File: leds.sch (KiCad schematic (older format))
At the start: 66 parts

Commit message: Remap project symbols
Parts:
- DB02, DB04, DB041, DB05, DB051, DB06, DB07, DB09, DB10, DB101, DB102, DB11, DB14, DB15, DB151, DB16, DB17, DB19, DB21, DB22, DB23, DB24, DB26, DB27, DB28, DB29, DB30, DB301, DB302, DB31, DB32, DB33, DB34, DB36, DB37, DB38, DB39, DB41, DB42, DB43, DB44, DB46, DB47, DB48, DB49, DB50, DB51, DB52, DB53, DB54, DB55, DB551, DB56, DB57, DB58, DB59, DB61, DB62, DB63, DB66, DB661, DB67, DB68, DB681, DB682, DB69: symbol LED -> device:LED
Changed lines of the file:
@@
-EESchema Schematic File Version 2
-LIBS:power
-LIBS:mx1a-simple
-LIBS:aker
-LIBS:atmega32u4
-LIBS:dtsjw
-LIBS:oupiin_usb
-LIBS:device
-LIBS:conn
-LIBS:keyboard-cache
-EELAYER 25 0
+EESchema Schematic File Version 4
+EELAYER 30 0
 EELAYER END
 $Descr A4 11693 8268
@@
 $EndDescr
 $Comp
-L LED DB21
+L device:LED DB21
 U 1 1 51900721
 P 4450 1950
@@
 $EndComp
 $Comp
-L LED DB26
+L device:LED DB26
 U 1 1 51900730
 P 5000 1950
@@
 $EndComp
 $Comp
-L LED DB31
+L device:LED DB31
 U 1 1 51900737
 P 5550 1950
@@
 $EndComp
 $Comp
-L LED DB36
+L device:LED DB36
 U 1 1 5190073E
 P 6100 1950
@@
 $EndComp
 $Comp
-L LED DB06
+L device:LED DB06
 U 1 1 5190074C
 P 2800 1950
@@
 $EndComp
 $Comp
-L LED DB11
+L device:LED DB11
 U 1 1 51900753
 P 3350 1950
@@
 $EndComp
 $Comp
-L LED DB16
+L device:LED DB16
 U 1 1 5190075A
 P 3900 1950
@@
 $EndComp
 $Comp
-L LED DB61
+L device:LED DB61
 U 1 1 51900761
 P 8850 1950
@@
 $EndComp
 $Comp
-L LED DB66
+L device:LED DB66
 U 1 1 51900768
 P 9400 1950
@@
 $EndComp
 $Comp
-L LED DB41
+L device:LED DB41
 U 1 1 5190077D
 P 6650 1950
@@
 $EndComp
 $Comp
-L LED DB46
+L device:LED DB46
 U 1 1 51900784
 P 7200 1950
@@
 $EndComp
 $Comp
-L LED DB51
+L device:LED DB51
 U 1 1 5190078B
 P 7750 1950
@@
 $EndComp
 $Comp
-L LED DB56
+L device:LED DB56
 U 1 1 51900792
 P 8300 1950
@@
 $EndComp
 $Comp
-L LED DB22
+L device:LED DB22
 U 1 1 51900799
 P 4450 2850
@@
 $EndComp
 $Comp
-L LED DB27
+L device:LED DB27
 U 1 1 519007A0
 P 5000 2850
@@
 $EndComp
 $Comp
-L LED DB32
+L device:LED DB32
 U 1 1 519007A7
 P 5550 2850
@@
 $EndComp
 $Comp
-L LED DB37
+L device:LED DB37
 U 1 1 519007AE
 P 6100 2850
@@
 $EndComp
 $Comp
-L LED DB02
+L device:LED DB02
 U 1 1 519007B5
 P 2250 2850
@@
 $EndComp
 $Comp
-L LED DB07
+L device:LED DB07
 U 1 1 519007BC
 P 2800 2850
@@
 $EndComp
 $Comp
-L LED DB17
+L device:LED DB17
 U 1 1 519007CA
 P 3900 2850
@@
 $EndComp
 $Comp
-L LED DB62
+L device:LED DB62
 U 1 1 519007D1
 P 8850 2850
@@
 $EndComp
 $Comp
-L LED DB67
+L device:LED DB67
 U 1 1 519007D8
 P 9400 2850
@@
 $EndComp
 $Comp
-L LED DB42
+L device:LED DB42
 U 1 1 519007E6
 P 6650 2850
@@
 $EndComp
 $Comp
-L LED DB47
+L device:LED DB47
 U 1 1 519007ED
 P 7200 2850
@@
 $EndComp
 $Comp
-L LED DB52
+L device:LED DB52
 U 1 1 519007F4
 P 7750 2850
@@
 $EndComp
 $Comp
-L LED DB57
+L device:LED DB57
 U 1 1 519007FB
 P 8300 2850
@@
 $EndComp
 $Comp
-L LED DB23
+L device:LED DB23
 U 1 1 51900802
 P 4450 3500
@@
 $EndComp
 $Comp
-L LED DB28
+L device:LED DB28
 U 1 1 51900809
 P 5000 3500
@@
 $EndComp
 $Comp
-L LED DB33
+L device:LED DB33
 U 1 1 51900810
 P 5550 3500
@@
 $EndComp
 $Comp
-L LED DB38
+L device:LED DB38
 U 1 1 51900817
 P 6100 3500
@@
 $EndComp
 $Comp
-L LED DB63
+L device:LED DB63
 U 1 1 5190083A
 P 8850 3500
@@
 $EndComp
 $Comp
-L LED DB68
+L device:LED DB68
 U 1 1 51900841
 P 9400 3500
@@
 $EndComp
 $Comp
-L LED DB43
+L device:LED DB43
 U 1 1 5190084F
 P 6650 3500
@@
 $EndComp
 $Comp
-L LED DB48
+L device:LED DB48
 U 1 1 51900856
 P 7200 3500
@@
 $EndComp
 $Comp
-L LED DB53
+L device:LED DB53
 U 1 1 5190085D
 P 7750 3500
@@
 $EndComp
 $Comp
-L LED DB58
+L device:LED DB58
 U 1 1 51900864
 P 8300 3500
@@
 $EndComp
 $Comp
-L LED DB24
+L device:LED DB24
 U 1 1 5190086B
 P 4450 4650
@@
 $EndComp
 $Comp
-L LED DB29
+L device:LED DB29
 U 1 1 51900872
 P 5000 4650
@@
 $EndComp
 $Comp
-L LED DB34
+L device:LED DB34
 U 1 1 51900879
 P 5550 4650
@@
 $EndComp
 $Comp
-L LED DB39
+L device:LED DB39
 U 1 1 51900880
 P 6100 4650
@@
 $EndComp
 $Comp
-L LED DB04
+L device:LED DB04
 U 1 1 51900887
 P 2250 4650
@@
 $EndComp
 $Comp
-L LED DB09
+L device:LED DB09
 U 1 1 5190088E
 P 2800 4650
@@
 $EndComp
 $Comp
-L LED DB14
+L device:LED DB14
 U 1 1 51900895
 P 3350 4650
@@
 $EndComp
 $Comp
-L LED DB19
+L device:LED DB19
 U 1 1 5190089C
 P 3900 4650
@@
 $EndComp
 $Comp
-L LED DB44
+L device:LED DB44
 U 1 1 519008B8
 P 6650 4650
@@
 $EndComp
 $Comp
-L LED DB49
+L device:LED DB49
 U 1 1 519008BF
 P 7200 4650
@@
 $EndComp
 $Comp
-L LED DB54
+L device:LED DB54
 U 1 1 519008C6
 P 7750 4650
@@
 $EndComp
 $Comp
-L LED DB59
+L device:LED DB59
 U 1 1 519008CD
 P 8300 4650
@@
 $EndComp
 $Comp
-L LED DB05
+L device:LED DB05
 U 1 1 519008F0
 P 2250 5550
@@
 $EndComp
 $Comp
-L LED DB10
+L device:LED DB10
 U 1 1 519008F7
 P 2800 5550
@@
 $EndComp
 $Comp
-L LED DB15
+L device:LED DB15
 U 1 1 519008FE
 P 3350 5550
@@
 $EndComp
 $Comp
-L LED DB50
+L device:LED DB50
 U 1 1 51900928
 P 7200 5550
@@
 $EndComp
 $Comp
-L LED DB55
+L device:LED DB55
 U 1 1 5190092F
 P 7750 5550
@@
 $EndComp
 $Comp
-L LED DB30
+L device:LED DB30
 U 1 1 519008DB
 P 5000 5550
@@
 $EndComp
 $Comp
-L LED DB551
+L device:LED DB551
 U 1 1 51C02CCF
 P 7750 5800
@@
 $EndComp
 $Comp
-L LED DB301
+L device:LED DB301
 U 1 1 51C0300D
 P 5000 5800
@@
 $EndComp
 $Comp
-L LED DB302
+L device:LED DB302
 U 1 1 51C03013
 P 5000 6050
@@
 $EndComp
 $Comp
-L LED DB051
+L device:LED DB051
 U 1 1 51C0378E
 P 2250 5800
@@
 $EndComp
 $Comp
-L LED DB101
+L device:LED DB101
 U 1 1 51C065B4
 P 2800 5800
@@
 $EndComp
 $Comp
-L LED DB102
+L device:LED DB102
 U 1 1 51C065BA
 P 2800 6050
@@
 $EndComp
 $Comp
-L LED DB151
+L device:LED DB151
 U 1 1 51C06955
 P 3350 5800
@@
 esc
 $Comp
-L LED DB69
+L device:LED DB69
 U 1 1 51C41A1A
 P 9400 4650
@@
 Fn
 $Comp
-L LED DB041
+L device:LED DB041
 U 1 1 51D98243
 P 2250 4900
@@
 Connection ~ 2050 4900
 $Comp
-L LED DB661
+L device:LED DB661
 U 1 1 51D9840C
 P 9400 2200
@@
 Connection ~ 9200 2200
 $Comp
-L LED DB681
+L device:LED DB681
 U 1 1 51D988E8
 P 9400 3750
@@
 $EndComp
 $Comp
-L LED DB682
+L device:LED DB682
 U 1 1 51D988EE
 P 9400 4000

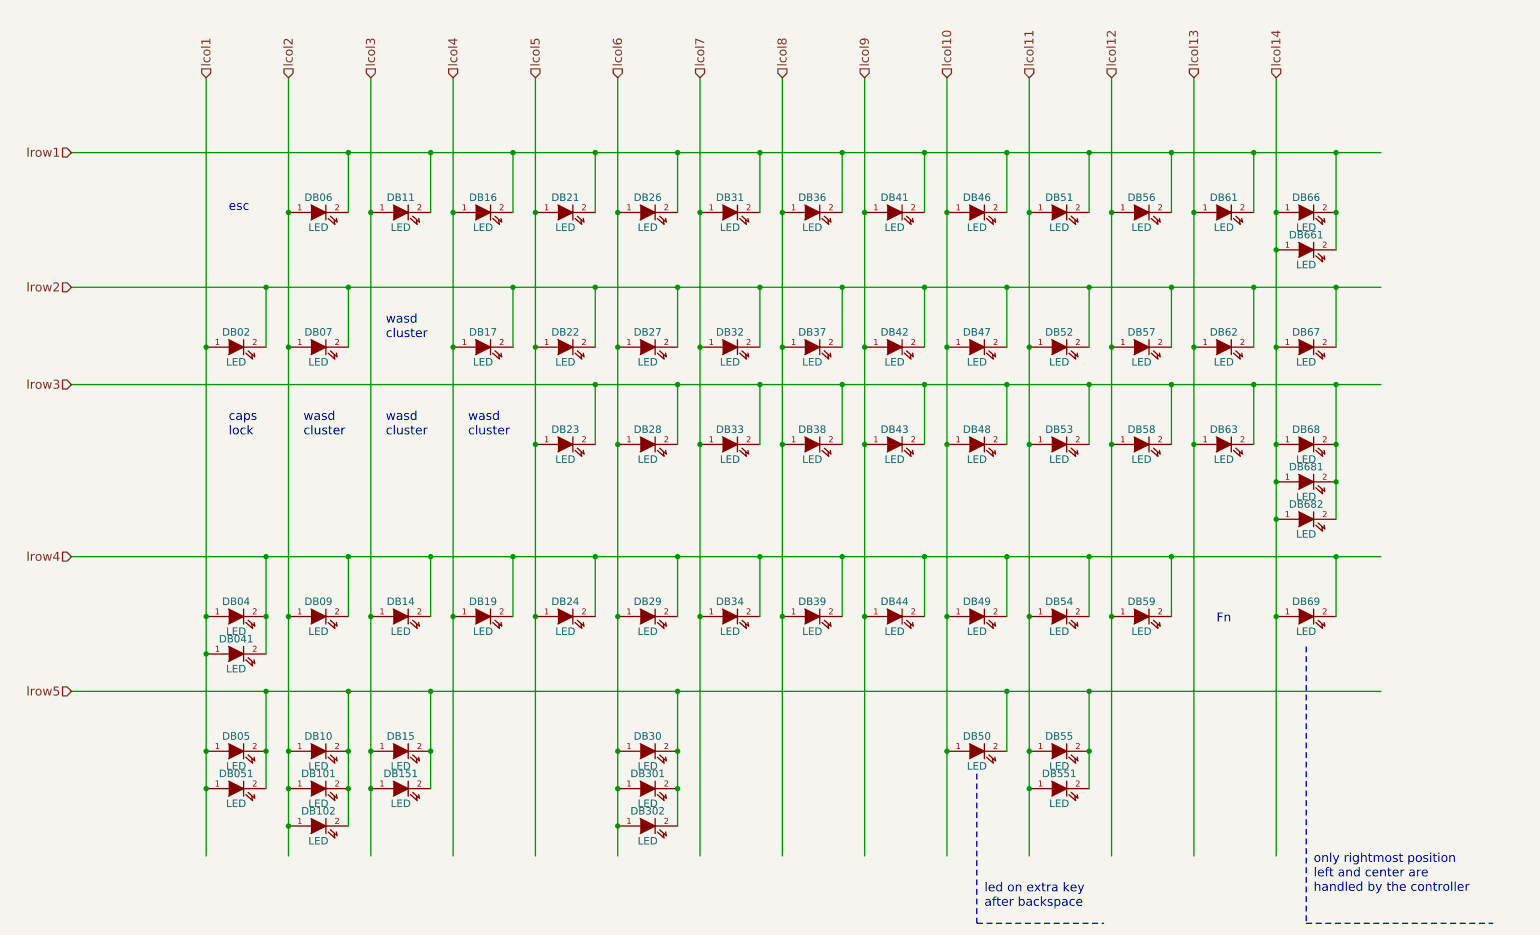
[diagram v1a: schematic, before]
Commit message: Remove SW50 from matrix and leds
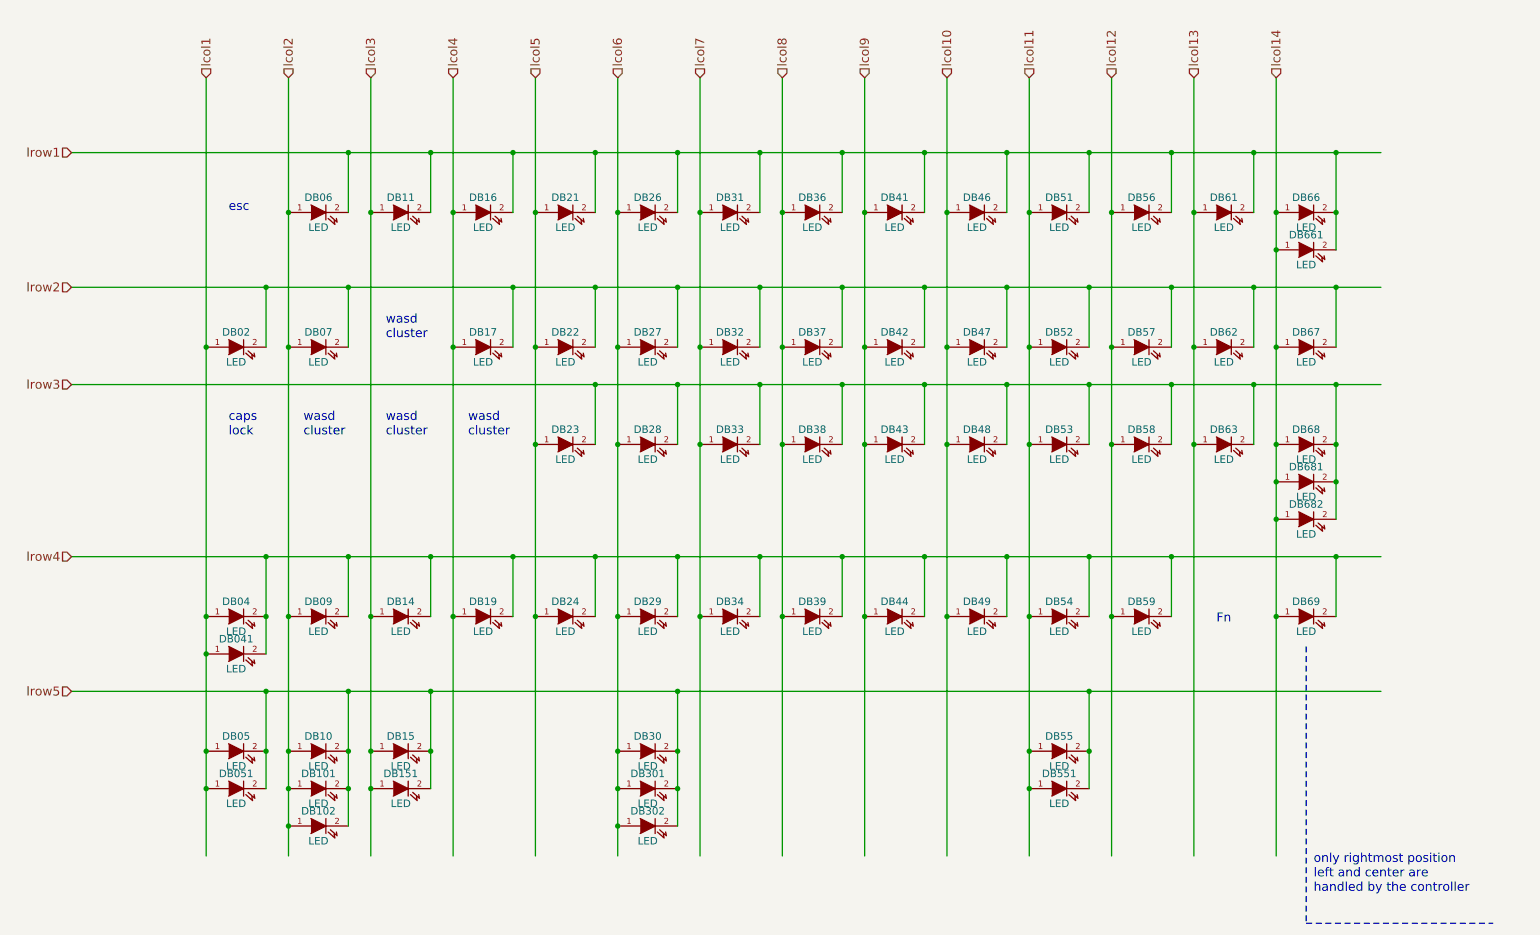
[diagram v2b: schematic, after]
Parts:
- removed DB50: LED, mx1a:MX1A-led_no3d, symbol device:LED
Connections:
- wire segments 74 -> 203
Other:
- note removed: "led on extra key\nafter backspace"

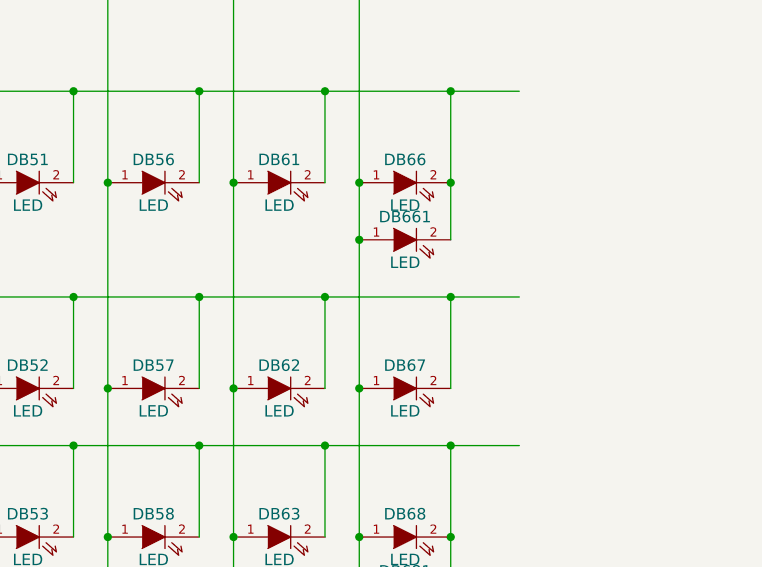
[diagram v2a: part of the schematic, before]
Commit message: Remove SW661
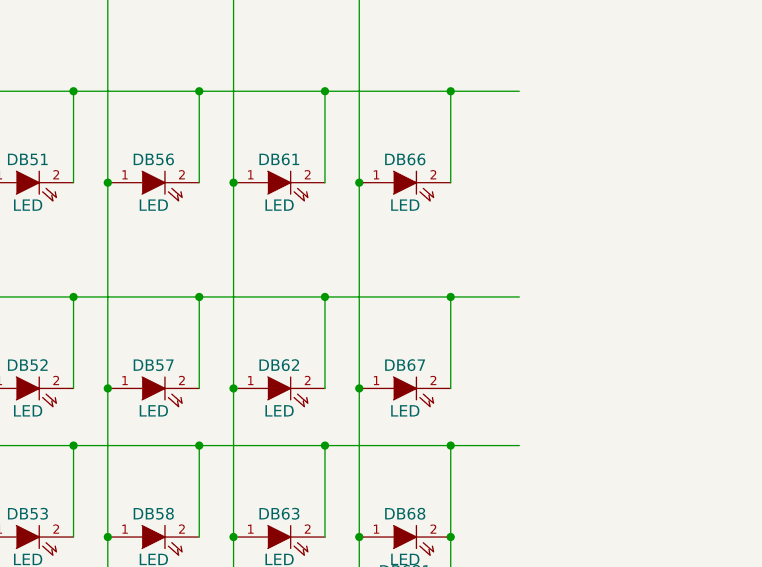
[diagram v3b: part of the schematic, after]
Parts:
- removed DB661: LED, mx1a:MX1A-led_no3d, symbol device:LED
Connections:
- wire segments 203 -> 201
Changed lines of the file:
@@
 Connection ~ 2050 4900
-$Comp
-L device:LED DB661
-U 1 1 51D9840C
-P 9400 2200
-F 0 "DB661" H 9400 2300 50  0000 C CNN
-F 1 "LED" H 9400 2100 50  0000 C CNN
-F 2 "mx1a:MX1A-led_no3d" H 9400 2200 60  0001 C CNN
-F 3 "" H 9400 2200 60  0001 C CNN
-	1    9400 2200
-	1    0    0    -1
-$EndComp
-Connection ~ 9600 1950
-Connection ~ 9200 2200
 $Comp
 L device:LED DB681
@@
 	9050 1550 9600 1550
 Wire Wire Line
-	9200 1950 9200 2200
-Wire Wire Line
 	9600 1550 9900 1550
 Wire Wire Line
@@
 	2050 4900 2050 5550
 Wire Wire Line
-	9600 1950 9600 2200
-Wire Wire Line
-	9200 2200 9200 2850
-Wire Wire Line
 	9600 3500 9600 3750
 Wire Wire Line
@@
 Wire Wire Line
 	5200 5150 7950 5150
+Wire Wire Line
+	9200 1950 9200 2850
 $EndSCHEMATC

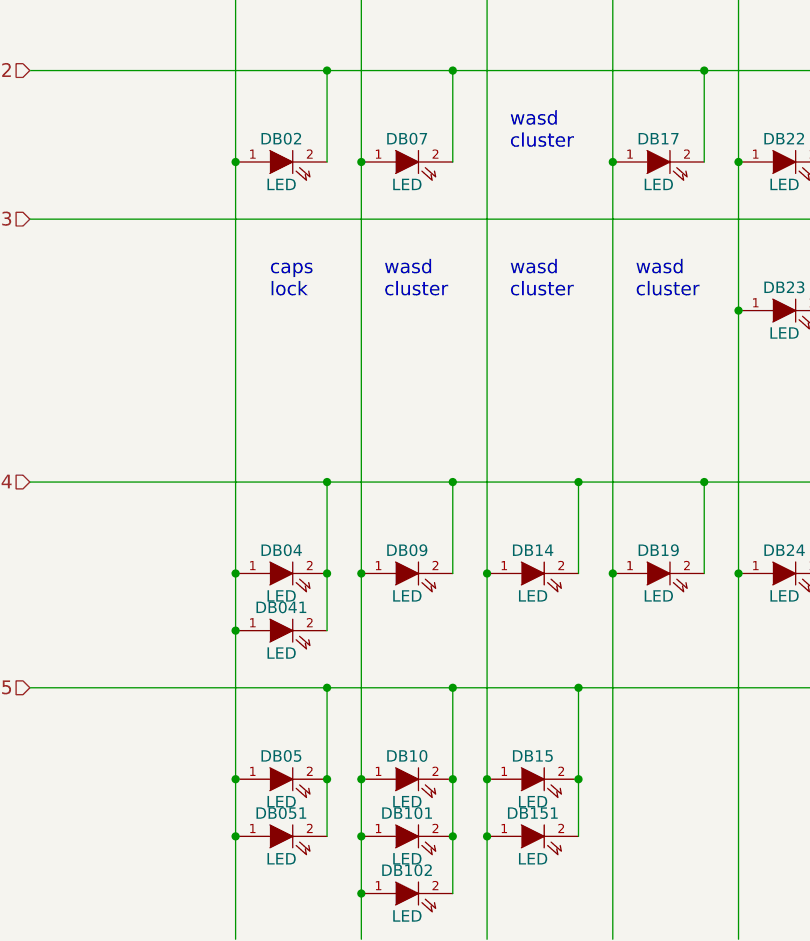
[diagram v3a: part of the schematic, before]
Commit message: Remove SW09 and SW041
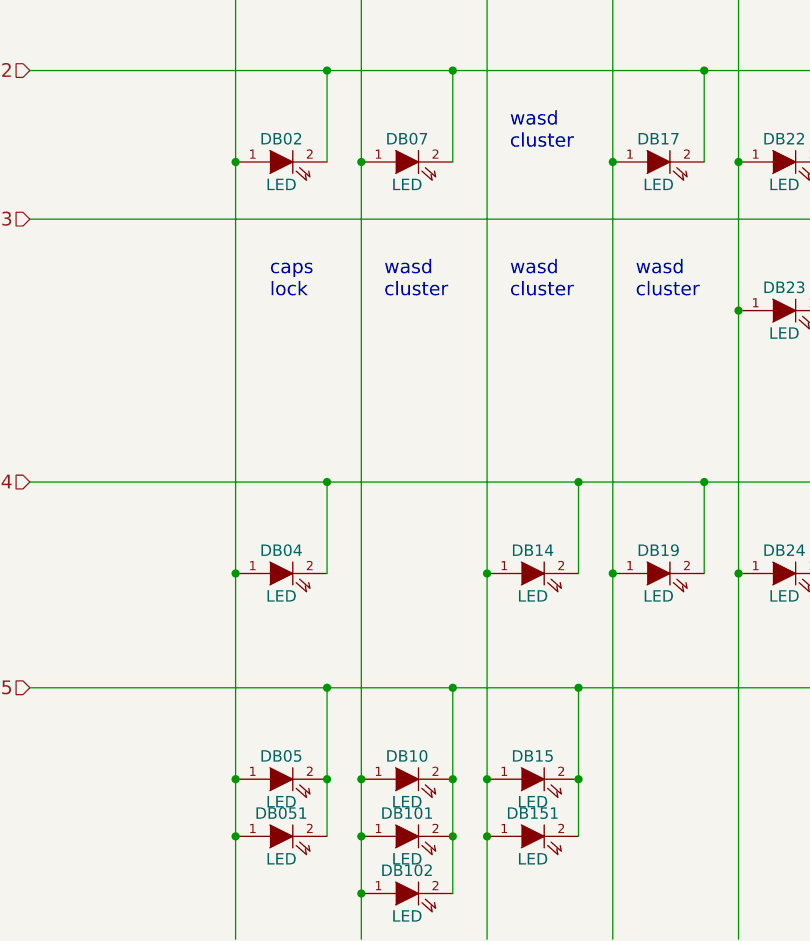
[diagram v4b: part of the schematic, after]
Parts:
- removed DB041, DB09: LED, mx1a:MX1A-led_no3d, symbol device:LED
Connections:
- wire segments 201 -> 196
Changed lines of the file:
@@
-$EndComp
-$Comp
-L device:LED DB09
-U 1 1 5190088E
-P 2800 4650
-F 0 "DB09" H 2800 4750 50  0000 C CNN
-F 1 "LED" H 2800 4550 50  0000 C CNN
-F 2 "mx1a:MX1A-led_no3d" H 2800 4650 60  0001 C CNN
-F 3 "" H 2800 4650 60  0001 C CNN
-	1    2800 4650
-	1    0    0    -1
 $EndComp
 $Comp
@@
 Wire Wire Line
 	2450 4250 2450 4650
-Wire Wire Line
-	3000 4250 3000 4650
 Wire Wire Line
 	3550 4250 3550 4650
@@
 Connection ~ 2050 4650
 Connection ~ 2450 4250
-Connection ~ 2600 4650
-Connection ~ 3000 4250
 Connection ~ 3150 4650
 Connection ~ 3550 4250
@@
 Fn
 $Comp
-L device:LED DB041
-U 1 1 51D98243
-P 2250 4900
-F 0 "DB041" H 2250 5000 50  0000 C CNN
-F 1 "LED" H 2250 4800 50  0000 C CNN
-F 2 "mx1a:MX1A-led_no3d" H 2250 4900 60  0001 C CNN
-F 3 "" H 2250 4900 60  0001 C CNN
-	1    2250 4900
-	1    0    0    -1
-$EndComp
-Connection ~ 2450 4650
-Connection ~ 2050 4900
-$Comp
 L device:LED DB681
 U 1 1 51D988E8
@@
 	2450 2450 3000 2450
 Wire Wire Line
-	2600 2850 2600 4650
-Wire Wire Line
 	3000 2450 4100 2450
 Wire Wire Line
@@
 	9600 2450 9900 2450
 Wire Wire Line
-	2050 4650 2050 4900
-Wire Wire Line
-	2450 4250 3000 4250
-Wire Wire Line
-	2600 4650 2600 5550
-Wire Wire Line
-	3000 4250 3550 4250
-Wire Wire Line
 	3150 4650 3150 5550
 Wire Wire Line
@@
 	9600 4250 9900 4250
 Wire Wire Line
-	2450 4650 2450 4900
-Wire Wire Line
-	2050 4900 2050 5550
-Wire Wire Line
 	9600 3500 9600 3750
 Wire Wire Line
@@
 Wire Wire Line
 	9200 1950 9200 2850
+Wire Wire Line
+	2600 2850 2600 5550
+Wire Wire Line
+	2450 4250 3550 4250
+Wire Wire Line
+	2050 4650 2050 5550
 $EndSCHEMATC

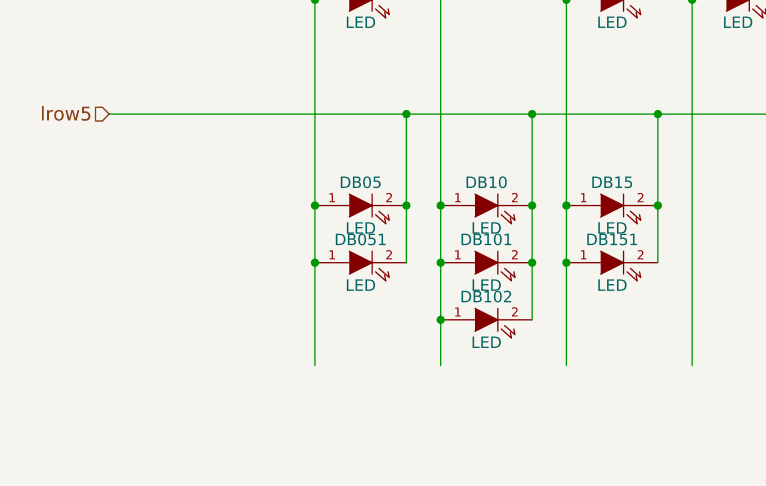
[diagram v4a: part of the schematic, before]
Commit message: Remove SW0512
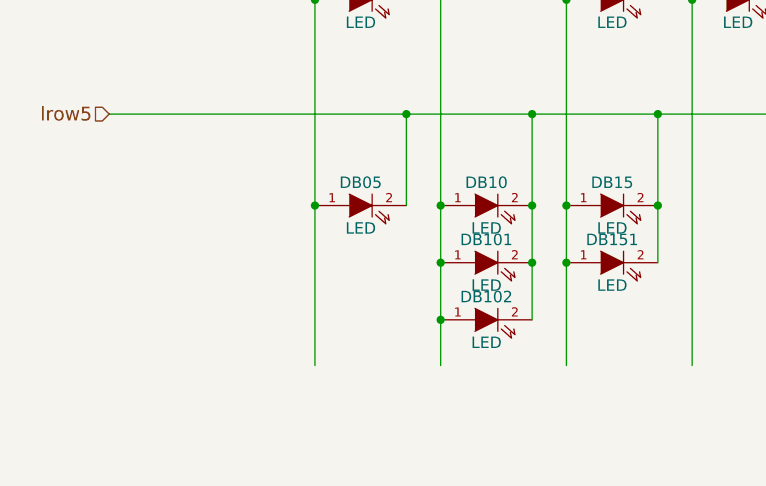
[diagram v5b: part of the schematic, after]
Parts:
- removed DB051: LED, symbol device:LED
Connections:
- wire segments 196 -> 194
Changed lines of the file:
@@
-$EndComp
-$Comp
-L device:LED DB051
-U 1 1 51C0378E
-P 2250 5800
-F 0 "DB051" H 2250 5900 50  0000 C CNN
-F 1 "LED" H 2250 5700 50  0000 C CNN
-F 2 "" H 2250 5800 60  0001 C CNN
-F 3 "" H 2250 5800 60  0001 C CNN
-	1    2250 5800
-	1    0    0    -1
 $EndComp
 $Comp
@@
 Connection ~ 4800 5800
 Connection ~ 4800 6050
-Connection ~ 2450 5550
-Connection ~ 2050 5800
 Connection ~ 3000 5550
 Connection ~ 3000 5800
@@
 	9600 3100 9900 3100
 Wire Wire Line
-	2050 5550 2050 5800
-Wire Wire Line
 	2450 5150 3000 5150
 Wire Wire Line
@@
 	4800 6050 4800 6250
 Wire Wire Line
-	2450 5550 2450 5800
-Wire Wire Line
-	2050 5800 2050 6250
-Wire Wire Line
 	3000 5550 3000 5800
 Wire Wire Line
@@
 Wire Wire Line
 	2050 4650 2050 5550
+Wire Wire Line
+	2050 5550 2050 6250
 $EndSCHEMATC
